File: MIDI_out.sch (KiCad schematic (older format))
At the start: 2 parts

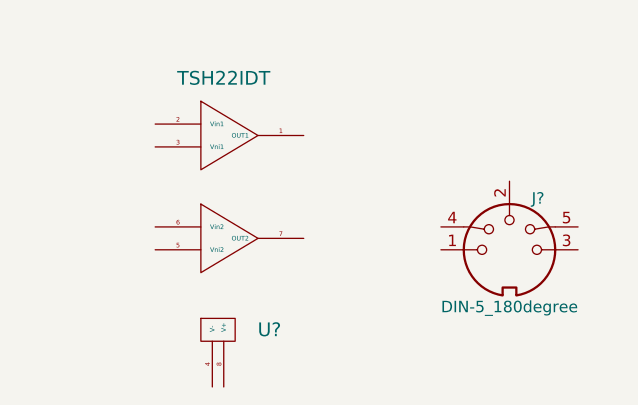
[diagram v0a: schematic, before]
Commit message: update to MIDI out sheet
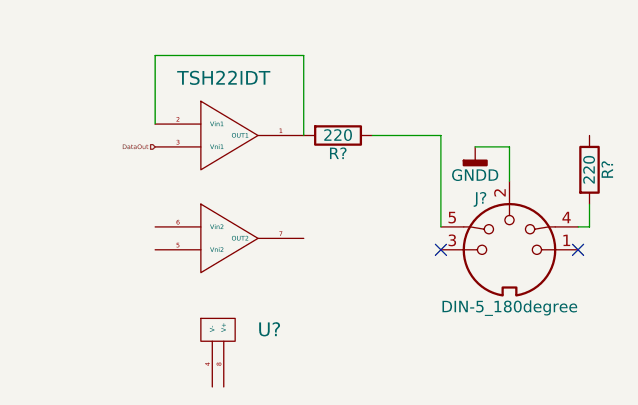
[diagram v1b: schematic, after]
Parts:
- added R? (x2): 220, symbol R
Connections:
- net GNDD: now reaches J?.2
- net at J?.4: now also R?.2
- net at J?.5: now also R?.1
- net at U?.1 (OUT1): now also U?.2 (Vin1), R?.2
- net DataOut: now reaches U?.3 (Vni1)
- no-connect marks 0 -> 2
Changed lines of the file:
@@
 LIBS:cmos4000
 LIBS:conn
-LIBS:logo
 LIBS:microchip_dspic33dsc
 LIBS:microchip_pic10mcu
@@
 LIBS:microchip_pic32mcu
 LIBS:msp430
-LIBS:MyLib
 LIBS:nxp_armmcu
 LIBS:relays
@@
 LIBS:ttl_ieee
 LIBS:valves
-LIBS:ac-dc
-LIBS:adc-dac
-LIBS:Altera
-LIBS:analog_devices
-LIBS:analog_switches
-LIBS:atmel
-LIBS:audio
-LIBS:Battery_Management
-LIBS:bbd
-LIBS:bosch
-LIBS:brooktre
-LIBS:Connector
-LIBS:contrib
-LIBS:cypress
-LIBS:dc-dc
-LIBS:device
-LIBS:digital-audio
-LIBS:Diode
-LIBS:Display
-LIBS:driver_gate
-LIBS:dsp
-LIBS:DSP_Microchip_DSPIC33
-LIBS:elec-unifil
-LIBS:ESD_Protection
-LIBS:Espressif
-LIBS:FPGA_Actel
-LIBS:ftdi
-LIBS:gennum
-LIBS:Graphic
-LIBS:hc11
-LIBS:infineon
-LIBS:intel
-LIBS:interface
-LIBS:intersil
-LIBS:ir
-LIBS:Lattice
-LIBS:LED
-LIBS:LEM
-LIBS:linear
-LIBS:Logic_74xgxx
-LIBS:Logic_74xx
-LIBS:Logic_CMOS_4000
-LIBS:Logic_CMOS_IEEE
-LIBS:logic_programmable
-LIBS:Logic_TTL_IEEE
-LIBS:maxim
-LIBS:MCU_Microchip_PIC10
-LIBS:MCU_Microchip_PIC12
-LIBS:MCU_Microchip_PIC16
-LIBS:MCU_Microchip_PIC18
-LIBS:MCU_Microchip_PIC24
-LIBS:MCU_Microchip_PIC32
-LIBS:MCU_NXP_Kinetis
-LIBS:MCU_NXP_LPC
-LIBS:MCU_NXP_S08
-LIBS:MCU_ST_STM8
-LIBS:MCU_ST_STM32
-LIBS:MCU_Texas_MSP430
-LIBS:Mechanical
-LIBS:memory
-LIBS:microchip
-LIBS:microcontrollers
-LIBS:modules
-LIBS:Motor
-LIBS:motor_drivers
-LIBS:motorola
-LIBS:nordicsemi
-LIBS:nxp
-LIBS:onsemi
-LIBS:opto
-LIBS:Oscillators
-LIBS:philips
-LIBS:power
-LIBS:Power_Management
-LIBS:powerint
-LIBS:pspice
-LIBS:references
-LIBS:regul
-LIBS:Relay
-LIBS:rfcom
-LIBS:RFSolutions
-LIBS:Sensor_Current
-LIBS:sensors
-LIBS:silabs
-LIBS:siliconi
-LIBS:supertex
-LIBS:Switch
-LIBS:texas
-LIBS:Transformer
-LIBS:Transistor
-LIBS:triac_thyristor
-LIBS:Valve
-LIBS:video
-LIBS:wiznet
-LIBS:Worldsemi
-LIBS:Xicor
-LIBS:xilinx
-LIBS:zetex
-LIBS:Zilog
 LIBS:Modulin-cache
 EELAYER 25 0
@@
 F 3 "" H 6100 3750 50  0001 C CNN
 	1    6100 3750
-	1    0    0    -1
+	-1   0    0    -1
 $EndComp
 $Comp
@@
 	1    0    0    -1
 $EndComp
+Wire Wire Line
+	4550 3200 4550 2900
+Wire Wire Line
+	4550 2900 5200 2900
+Wire Wire Line
+	5200 2900 5200 3250
+$Comp
+L R R?
+U 1 1 5A148F21
+P 5350 3250
+F 0 "R?" V 5430 3250 50  0000 C CNN
+F 1 "220" V 5350 3250 50  0000 C CNN
+F 2 "" V 5280 3250 50  0001 C CNN
+F 3 "" H 5350 3250 50  0001 C CNN
+	1    5350 3250
+	0    1    1    0
+$EndComp
+Wire Wire Line
+	5500 3250 5800 3250
+Wire Wire Line
+	5800 3250 5800 3650
+$Comp
+L GNDD #PWR?
+U 1 1 5A14901A
+P 5950 3300
+F 0 "#PWR?" H 5950 3050 50  0001 C CNN
+F 1 "GNDD" H 5950 3175 50  0000 C CNN
+F 2 "" H 5950 3300 50  0001 C CNN
+F 3 "" H 5950 3300 50  0001 C CNN
+	1    5950 3300
+	1    0    0    -1
+$EndComp
+Wire Wire Line
+	5950 3300 6100 3300
+Wire Wire Line
+	6100 3300 6100 3450
+$Comp
+L R R?
+U 1 1 5A14909D
+P 6450 3400
+F 0 "R?" V 6530 3400 50  0000 C CNN
+F 1 "220" V 6450 3400 50  0000 C CNN
+F 2 "" V 6380 3400 50  0001 C CNN
+F 3 "" H 6450 3400 50  0001 C CNN
+	1    6450 3400
+	1    0    0    -1
+$EndComp
+Wire Wire Line
+	6400 3650 6450 3650
+Wire Wire Line
+	6450 3650 6450 3550
+Text HLabel 4550 3300 0    20   Input ~ 0
+DataOut
+NoConn ~ 6400 3750
+NoConn ~ 5800 3750
 $EndSCHEMATC

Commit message: Added circuit for encoder
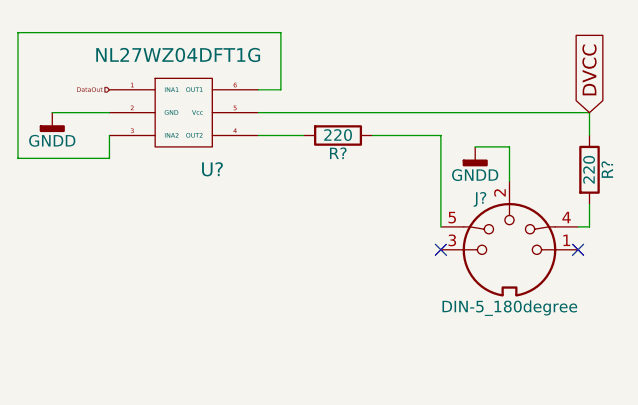
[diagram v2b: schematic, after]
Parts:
- removed U?: TSH22IDT, symbol TSH22IDT
- added U?: NL27WZ04DFT1G, symbol NL27WZ04DFT1G
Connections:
- net DataOut: now also U?.1 (INA1)
- net GNDD: now also U?.2 (GND)
- net at R?.2: now also U?.4 (OUT2)
- net DVCC: now reaches R?.1
- net DVCC: now also U?.5 (Vcc)
- new net: U?.3 (INA2), U?.6 (OUT1)
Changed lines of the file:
@@
 LIBS:74xgxx
 LIBS:74xx
+LIBS:ac-dc
 LIBS:actel
+LIBS:adc-dac
+LIBS:allegro
+LIBS:Altera
+LIBS:analog_devices
+LIBS:analog_switches
+LIBS:atmel
+LIBS:audio
+LIBS:battery_management
+LIBS:bbd
+LIBS:bosch
+LIBS:brooktre
 LIBS:cmos_ieee
 LIBS:cmos4000
 LIBS:conn
+LIBS:contrib
+LIBS:cypress
+LIBS:dc-dc
+LIBS:device
+LIBS:digital-audio
+LIBS:diode
+LIBS:display
+LIBS:dsp
+LIBS:elec-unifil
+LIBS:ESD_Protection
+LIBS:ftdi
+LIBS:gennum
+LIBS:graphic_symbols
+LIBS:hc11
+LIBS:infineon
+LIBS:intel
+LIBS:interface
+LIBS:intersil
+LIBS:ir
+LIBS:Lattice
+LIBS:leds
+LIBS:LEM
+LIBS:linear
+LIBS:logic_programmable
+LIBS:maxim
+LIBS:mechanical
+LIBS:memory
+LIBS:microchip
 LIBS:microchip_dspic33dsc
 LIBS:microchip_pic10mcu
@@
 LIBS:microchip_pic16mcu
 LIBS:microchip_pic18mcu
+LIBS:microchip_pic24mcu
 LIBS:microchip_pic32mcu
+LIBS:microcontrollers
+LIBS:modules
+LIBS:motor_drivers
+LIBS:motorola
+LIBS:motors
 LIBS:msp430
+LIBS:nordicsemi
+LIBS:nxp
 LIBS:nxp_armmcu
+LIBS:onsemi
+LIBS:opto
+LIBS:Oscillators
+LIBS:philips
+LIBS:power
+LIBS:Power_Management
+LIBS:powerint
+LIBS:pspice
+LIBS:references
+LIBS:regul
 LIBS:relays
+LIBS:rfcom
+LIBS:RFSolutions
+LIBS:sensors
+LIBS:silabs
+LIBS:siliconi
 LIBS:stm8
 LIBS:stm32
+LIBS:supertex
 LIBS:switches
+LIBS:texas
 LIBS:transf
 LIBS:transistors
+LIBS:triac_thyristor
 LIBS:ttl_ieee
 LIBS:valves
+LIBS:video
+LIBS:wiznet
+LIBS:Worldsemi
+LIBS:Xicor
+LIBS:xilinx
+LIBS:zetex
+LIBS:Zilog
 LIBS:Modulin-cache
 EELAYER 25 0
@@
 $Descr A4 11693 8268
 encoding utf-8
-Sheet 4 4
+Sheet 4 5
 Title ""
 Date ""
@@
 $EndComp
 $Comp
-L TSH22IDT U?
-U 1 1 5A18B7B7
-P 4750 3250
-F 0 "U?" H 5050 2400 60  0000 C CNN
-F 1 "TSH22IDT" H 4850 3500 60  0000 C CNN
-F 2 "" H 4750 3250 60  0001 C CNN
-F 3 "" H 4750 3250 60  0001 C CNN
-	1    4750 3250
-	1    0    0    -1
-$EndComp
-Wire Wire Line
-	4550 3200 4550 2900
-Wire Wire Line
-	4550 2900 5200 2900
-Wire Wire Line
-	5200 2900 5200 3250
-$Comp
 L R R?
 U 1 1 5A148F21
@@
 Wire Wire Line
 	6450 3650 6450 3550
-Text HLabel 4550 3300 0    20   Input ~ 0
+Text HLabel 4350 3050 0    20   Input ~ 0
 DataOut
 NoConn ~ 6400 3750
 NoConn ~ 5800 3750
+$Comp
+L NL27WZ04DFT1G U?
+U 1 1 5A1596F2
+P 4650 3150
+F 0 "U?" H 4800 2900 60  0000 C CNN
+F 1 "NL27WZ04DFT1G" H 4650 3400 60  0000 C CNN
+F 2 "" H 4650 3200 60  0001 C CNN
+F 3 "" H 4650 3200 60  0001 C CNN
+	1    4650 3150
+	1    0    0    -1
+$EndComp
+$Comp
+L GNDD #PWR?
+U 1 1 5A159789
+P 4100 3150
+F 0 "#PWR?" H 4100 2900 50  0001 C CNN
+F 1 "GNDD" H 4100 3025 50  0000 C CNN
+F 2 "" H 4100 3150 50  0001 C CNN
+F 3 "" H 4100 3150 50  0001 C CNN
+	1    4100 3150
+	1    0    0    -1
+$EndComp
+Wire Wire Line
+	4100 3150 4350 3150
+Wire Wire Line
+	5000 3050 5100 3050
+Wire Wire Line
+	5100 3050 5100 2800
+Wire Wire Line
+	5100 2800 3950 2800
+Wire Wire Line
+	3950 2800 3950 3350
+Wire Wire Line
+	3950 3350 4350 3350
+Wire Wire Line
+	4350 3350 4350 3250
+Wire Wire Line
+	5000 3250 5200 3250
+Wire Wire Line
+	5000 3150 6450 3150
+Wire Wire Line
+	6450 3150 6450 3250
+Text GLabel 6450 3150 1    60   Input ~ 0
+DVCC
 $EndSCHEMATC

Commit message: Finished Rev1 schematic and assigned most footprints
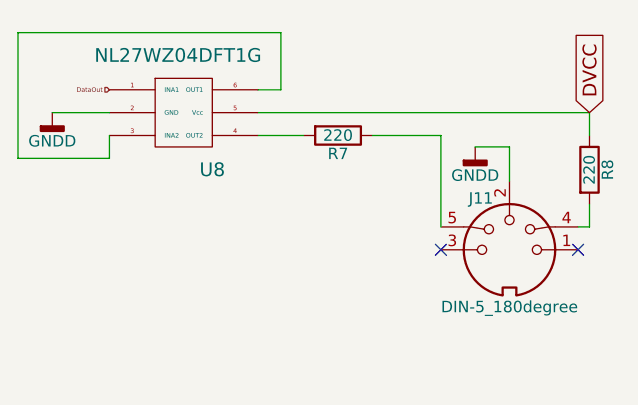
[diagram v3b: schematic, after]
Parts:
- R7, R8: renamed from R?; footprint (none) -> Resistors_SMD:R_0603
- U8: renamed from U?; footprint (none) -> TO_SOT_Packages_SMD:SOT-363_SC-70-6
- gave numbers to parts that had none: 1
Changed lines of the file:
@@
 EESchema Schematic File Version 2
-LIBS:74xgxx
-LIBS:74xx
+LIBS:MyLib
 LIBS:ac-dc
-LIBS:actel
 LIBS:adc-dac
-LIBS:allegro
 LIBS:Altera
 LIBS:analog_devices
@@
 LIBS:atmel
 LIBS:audio
-LIBS:battery_management
+LIBS:Battery_Management
 LIBS:bbd
 LIBS:bosch
 LIBS:brooktre
-LIBS:cmos_ieee
-LIBS:cmos4000
-LIBS:conn
+LIBS:Connector
 LIBS:contrib
 LIBS:cypress
@@
 LIBS:device
 LIBS:digital-audio
-LIBS:diode
-LIBS:display
+LIBS:Diode
+LIBS:Display
+LIBS:driver_gate
 LIBS:dsp
+LIBS:DSP_Microchip_DSPIC33
 LIBS:elec-unifil
 LIBS:ESD_Protection
+LIBS:Espressif
+LIBS:FPGA_Actel
 LIBS:ftdi
 LIBS:gennum
-LIBS:graphic_symbols
+LIBS:Graphic
 LIBS:hc11
 LIBS:infineon
@@
 LIBS:ir
 LIBS:Lattice
-LIBS:leds
+LIBS:LED
 LIBS:LEM
 LIBS:linear
+LIBS:Logic_74xgxx
+LIBS:Logic_74xx
+LIBS:Logic_CMOS_4000
+LIBS:Logic_CMOS_IEEE
 LIBS:logic_programmable
+LIBS:Logic_TTL_IEEE
 LIBS:maxim
-LIBS:mechanical
+LIBS:MCU_Microchip_PIC10
+LIBS:MCU_Microchip_PIC12
+LIBS:MCU_Microchip_PIC16
+LIBS:MCU_Microchip_PIC18
+LIBS:MCU_Microchip_PIC24
+LIBS:MCU_Microchip_PIC32
+LIBS:MCU_NXP_Kinetis
+LIBS:MCU_NXP_LPC
+LIBS:MCU_NXP_S08
+LIBS:MCU_ST_STM8
+LIBS:MCU_ST_STM32
+LIBS:MCU_Texas_MSP430
+LIBS:Mechanical
 LIBS:memory
 LIBS:microchip
-LIBS:microchip_dspic33dsc
-LIBS:microchip_pic10mcu
-LIBS:microchip_pic12mcu
-LIBS:microchip_pic16mcu
-LIBS:microchip_pic18mcu
-LIBS:microchip_pic24mcu
-LIBS:microchip_pic32mcu
 LIBS:microcontrollers
 LIBS:modules
+LIBS:Motor
 LIBS:motor_drivers
 LIBS:motorola
-LIBS:motors
-LIBS:msp430
 LIBS:nordicsemi
 LIBS:nxp
-LIBS:nxp_armmcu
 LIBS:onsemi
 LIBS:opto
@@
 LIBS:references
 LIBS:regul
-LIBS:relays
+LIBS:Relay
 LIBS:rfcom
 LIBS:RFSolutions
+LIBS:Sensor_Current
 LIBS:sensors
 LIBS:silabs
 LIBS:siliconi
-LIBS:stm8
-LIBS:stm32
 LIBS:supertex
-LIBS:switches
+LIBS:Switch
 LIBS:texas
-LIBS:transf
-LIBS:transistors
+LIBS:Transformer
+LIBS:Transistor
 LIBS:triac_thyristor
-LIBS:ttl_ieee
-LIBS:valves
+LIBS:Valve
 LIBS:video
 LIBS:wiznet
@@
 LIBS:zetex
 LIBS:Zilog
+LIBS:74xgxx
+LIBS:74xx
+LIBS:actel
+LIBS:cmos_ieee
+LIBS:cmos4000
+LIBS:conn
+LIBS:logo
+LIBS:microchip_dspic33dsc
+LIBS:microchip_pic10mcu
+LIBS:microchip_pic12mcu
+LIBS:microchip_pic16mcu
+LIBS:microchip_pic18mcu
+LIBS:microchip_pic32mcu
+LIBS:msp430
+LIBS:nxp_armmcu
+LIBS:relays
+LIBS:stm8
+LIBS:stm32
+LIBS:switches
+LIBS:transf
+LIBS:transistors
+LIBS:ttl_ieee
+LIBS:valves
 LIBS:Modulin-cache
 EELAYER 25 0
@@
 $Descr A4 11693 8268
 encoding utf-8
-Sheet 4 5
+Sheet 4 6
 Title ""
 Date ""
@@
 $EndDescr
 $Comp
-L DIN-5_180degree J?
+L DIN-5_180degree J11
 U 1 1 5A18B7B0
 P 6100 3750
-F 0 "J?" H 6225 3975 50  0000 C CNN
+F 0 "J11" H 6225 3975 50  0000 C CNN
 F 1 "DIN-5_180degree" H 6100 3500 50  0000 C CNN
 F 2 "" H 6100 3750 50  0001 C CNN
@@
 $EndComp
 $Comp
-L R R?
+L R R7
 U 1 1 5A148F21
 P 5350 3250
-F 0 "R?" V 5430 3250 50  0000 C CNN
+F 0 "R7" V 5430 3250 50  0000 C CNN
 F 1 "220" V 5350 3250 50  0000 C CNN
-F 2 "" V 5280 3250 50  0001 C CNN
+F 2 "Resistors_SMD:R_0603" V 5280 3250 50  0001 C CNN
 F 3 "" H 5350 3250 50  0001 C CNN
 	1    5350 3250
@@
 	5800 3250 5800 3650
 $Comp
-L GNDD #PWR?
+L GNDD #PWR027
 U 1 1 5A14901A
 P 5950 3300
-F 0 "#PWR?" H 5950 3050 50  0001 C CNN
+F 0 "#PWR027" H 5950 3050 50  0001 C CNN
 F 1 "GNDD" H 5950 3175 50  0000 C CNN
 F 2 "" H 5950 3300 50  0001 C CNN
@@
 	6100 3300 6100 3450
 $Comp
-L R R?
+L R R8
 U 1 1 5A14909D
 P 6450 3400
-F 0 "R?" V 6530 3400 50  0000 C CNN
+F 0 "R8" V 6530 3400 50  0000 C CNN
 F 1 "220" V 6450 3400 50  0000 C CNN
-F 2 "" V 6380 3400 50  0001 C CNN
+F 2 "Resistors_SMD:R_0603" V 6380 3400 50  0001 C CNN
 F 3 "" H 6450 3400 50  0001 C CNN
 	1    6450 3400
@@
 NoConn ~ 5800 3750
 $Comp
-L NL27WZ04DFT1G U?
+L NL27WZ04DFT1G U8
 U 1 1 5A1596F2
 P 4650 3150
-F 0 "U?" H 4800 2900 60  0000 C CNN
+F 0 "U8" H 4800 2900 60  0000 C CNN
 F 1 "NL27WZ04DFT1G" H 4650 3400 60  0000 C CNN
-F 2 "" H 4650 3200 60  0001 C CNN
+F 2 "TO_SOT_Packages_SMD:SOT-363_SC-70-6" H 4650 3200 60  0001 C CNN
 F 3 "" H 4650 3200 60  0001 C CNN
 	1    4650 3150
@@
 $EndComp
 $Comp
-L GNDD #PWR?
+L GNDD #PWR028
 U 1 1 5A159789
 P 4100 3150
-F 0 "#PWR?" H 4100 2900 50  0001 C CNN
+F 0 "#PWR028" H 4100 2900 50  0001 C CNN
 F 1 "GNDD" H 4100 3025 50  0000 C CNN
 F 2 "" H 4100 3150 50  0001 C CNN

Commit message: Halfway through layout. Started libraries.
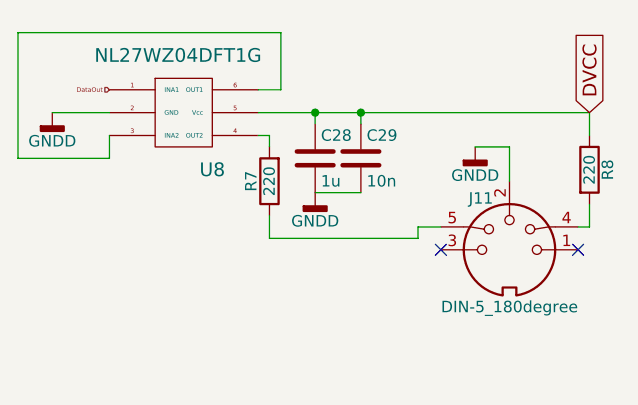
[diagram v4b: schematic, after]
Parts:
- added C28: 1u, Capacitors_SMD:C_0603, symbol C
- added C29: 10n, Capacitors_SMD:C_0603, symbol C
- J11: footprint (none) -> Modulin:SDS-50J
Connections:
- net DVCC: now also C28.1, C29.1
- net GNDD: now also C28.2, C29.2
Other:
- moved on the sheet: R7
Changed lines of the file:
@@
 EESchema Schematic File Version 2
-LIBS:MyLib
+LIBS:74xgxx
+LIBS:74xx
 LIBS:ac-dc
+LIBS:actel
 LIBS:adc-dac
+LIBS:allegro
 LIBS:Altera
 LIBS:analog_devices
@@
 LIBS:atmel
 LIBS:audio
-LIBS:Battery_Management
+LIBS:battery_management
 LIBS:bbd
 LIBS:bosch
 LIBS:brooktre
-LIBS:Connector
+LIBS:cmos_ieee
+LIBS:cmos4000
+LIBS:conn
 LIBS:contrib
 LIBS:cypress
@@
 LIBS:device
 LIBS:digital-audio
-LIBS:Diode
-LIBS:Display
-LIBS:driver_gate
+LIBS:diode
+LIBS:display
 LIBS:dsp
-LIBS:DSP_Microchip_DSPIC33
 LIBS:elec-unifil
 LIBS:ESD_Protection
-LIBS:Espressif
-LIBS:FPGA_Actel
 LIBS:ftdi
 LIBS:gennum
-LIBS:Graphic
+LIBS:graphic_symbols
 LIBS:hc11
 LIBS:infineon
@@
 LIBS:ir
 LIBS:Lattice
-LIBS:LED
+LIBS:leds
 LIBS:LEM
 LIBS:linear
-LIBS:Logic_74xgxx
-LIBS:Logic_74xx
-LIBS:Logic_CMOS_4000
-LIBS:Logic_CMOS_IEEE
 LIBS:logic_programmable
-LIBS:Logic_TTL_IEEE
 LIBS:maxim
-LIBS:MCU_Microchip_PIC10
-LIBS:MCU_Microchip_PIC12
-LIBS:MCU_Microchip_PIC16
-LIBS:MCU_Microchip_PIC18
-LIBS:MCU_Microchip_PIC24
-LIBS:MCU_Microchip_PIC32
-LIBS:MCU_NXP_Kinetis
-LIBS:MCU_NXP_LPC
-LIBS:MCU_NXP_S08
-LIBS:MCU_ST_STM8
-LIBS:MCU_ST_STM32
-LIBS:MCU_Texas_MSP430
-LIBS:Mechanical
+LIBS:mechanical
 LIBS:memory
 LIBS:microchip
+LIBS:microchip_dspic33dsc
+LIBS:microchip_pic10mcu
+LIBS:microchip_pic12mcu
+LIBS:microchip_pic16mcu
+LIBS:microchip_pic18mcu
+LIBS:microchip_pic24mcu
+LIBS:microchip_pic32mcu
 LIBS:microcontrollers
 LIBS:modules
-LIBS:Motor
 LIBS:motor_drivers
 LIBS:motorola
+LIBS:motors
+LIBS:msp430
 LIBS:nordicsemi
 LIBS:nxp
+LIBS:nxp_armmcu
 LIBS:onsemi
 LIBS:opto
@@
 LIBS:references
 LIBS:regul
-LIBS:Relay
+LIBS:relays
 LIBS:rfcom
 LIBS:RFSolutions
-LIBS:Sensor_Current
 LIBS:sensors
 LIBS:silabs
 LIBS:siliconi
+LIBS:stm8
+LIBS:stm32
 LIBS:supertex
-LIBS:Switch
+LIBS:switches
 LIBS:texas
-LIBS:Transformer
-LIBS:Transistor
+LIBS:transf
+LIBS:transistors
 LIBS:triac_thyristor
-LIBS:Valve
+LIBS:ttl_ieee
+LIBS:valves
 LIBS:video
 LIBS:wiznet
@@
 LIBS:zetex
 LIBS:Zilog
-LIBS:74xgxx
-LIBS:74xx
-LIBS:actel
-LIBS:cmos_ieee
-LIBS:cmos4000
-LIBS:conn
-LIBS:logo
-LIBS:microchip_dspic33dsc
-LIBS:microchip_pic10mcu
-LIBS:microchip_pic12mcu
-LIBS:microchip_pic16mcu
-LIBS:microchip_pic18mcu
-LIBS:microchip_pic32mcu
-LIBS:msp430
-LIBS:nxp_armmcu
-LIBS:relays
-LIBS:stm8
-LIBS:stm32
-LIBS:switches
-LIBS:transf
-LIBS:transistors
-LIBS:ttl_ieee
-LIBS:valves
+LIBS:MyLib
 LIBS:Modulin-cache
 EELAYER 25 0
@@
 F 0 "J11" H 6225 3975 50  0000 C CNN
 F 1 "DIN-5_180degree" H 6100 3500 50  0000 C CNN
-F 2 "" H 6100 3750 50  0001 C CNN
+F 2 "Modulin:SDS-50J" H 6100 3750 50  0001 C CNN
 F 3 "" H 6100 3750 50  0001 C CNN
 	1    6100 3750
@@
 L R R7
 U 1 1 5A148F21
-P 5350 3250
-F 0 "R7" V 5430 3250 50  0000 C CNN
-F 1 "220" V 5350 3250 50  0000 C CNN
-F 2 "Resistors_SMD:R_0603" V 5280 3250 50  0001 C CNN
-F 3 "" H 5350 3250 50  0001 C CNN
-	1    5350 3250
-	0    1    1    0
-$EndComp
-Wire Wire Line
-	5500 3250 5800 3250
-Wire Wire Line
-	5800 3250 5800 3650
-$Comp
-L GNDD #PWR027
+P 5050 3450
+F 0 "R7" V 5130 3450 50  0000 C CNN
+F 1 "220" V 5050 3450 50  0000 C CNN
+F 2 "Resistors_SMD:R_0603" V 4980 3450 50  0001 C CNN
+F 3 "" H 5050 3450 50  0001 C CNN
+	1    5050 3450
+	-1   0    0    1
+$EndComp
+$Comp
+L GNDD #PWR033
 U 1 1 5A14901A
 P 5950 3300
-F 0 "#PWR027" H 5950 3050 50  0001 C CNN
+F 0 "#PWR033" H 5950 3050 50  0001 C CNN
 F 1 "GNDD" H 5950 3175 50  0000 C CNN
 F 2 "" H 5950 3300 50  0001 C CNN
@@
 $EndComp
 $Comp
-L GNDD #PWR028
+L GNDD #PWR034
 U 1 1 5A159789
 P 4100 3150
-F 0 "#PWR028" H 4100 2900 50  0001 C CNN
+F 0 "#PWR034" H 4100 2900 50  0001 C CNN
 F 1 "GNDD" H 4100 3025 50  0000 C CNN
 F 2 "" H 4100 3150 50  0001 C CNN
@@
 	4350 3350 4350 3250
 Wire Wire Line
-	5000 3250 5200 3250
+	5000 3250 5050 3250
 Wire Wire Line
 	5000 3150 6450 3150
@@
 Text GLabel 6450 3150 1    60   Input ~ 0
 DVCC
+Wire Wire Line
+	5050 3700 5700 3700
+$Comp
+L C C28
+U 1 1 5A18AAA3
+P 5250 3350
+F 0 "C28" H 5275 3450 50  0000 L CNN
+F 1 "1u" H 5275 3250 50  0000 L CNN
+F 2 "Capacitors_SMD:C_0603" H 5288 3200 50  0001 C CNN
+F 3 "" H 5250 3350 50  0001 C CNN
+	1    5250 3350
+	1    0    0    -1
+$EndComp
+Wire Wire Line
+	5250 3200 5250 3150
+Connection ~ 5250 3150
+Wire Wire Line
+	5050 3250 5050 3300
+Wire Wire Line
+	5050 3600 5050 3700
+$Comp
+L C C29
+U 1 1 5A18AB80
+P 5450 3350
+F 0 "C29" H 5475 3450 50  0000 L CNN
+F 1 "10n" H 5475 3250 50  0000 L CNN
+F 2 "Capacitors_SMD:C_0603" H 5488 3200 50  0001 C CNN
+F 3 "" H 5450 3350 50  0001 C CNN
+	1    5450 3350
+	1    0    0    -1
+$EndComp
+Wire Wire Line
+	5450 3200 5450 3150
+Connection ~ 5450 3150
+$Comp
+L GNDD #PWR035
+U 1 1 5A18ABCD
+P 5250 3500
+F 0 "#PWR035" H 5250 3250 50  0001 C CNN
+F 1 "GNDD" H 5250 3375 50  0000 C CNN
+F 2 "" H 5250 3500 50  0001 C CNN
+F 3 "" H 5250 3500 50  0001 C CNN
+	1    5250 3500
+	1    0    0    -1
+$EndComp
+Wire Wire Line
+	5450 3500 5250 3500
+Wire Wire Line
+	5700 3700 5700 3650
+Wire Wire Line
+	5700 3650 5800 3650
 $EndSCHEMATC
